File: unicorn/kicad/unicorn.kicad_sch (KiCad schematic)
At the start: 25 parts, among them J1 Conn_01x02, J2 SPI, J3 Conn_01x14_Female, J4 Conn_01x14_Female, U1 L7805, U2 ATmega328-P

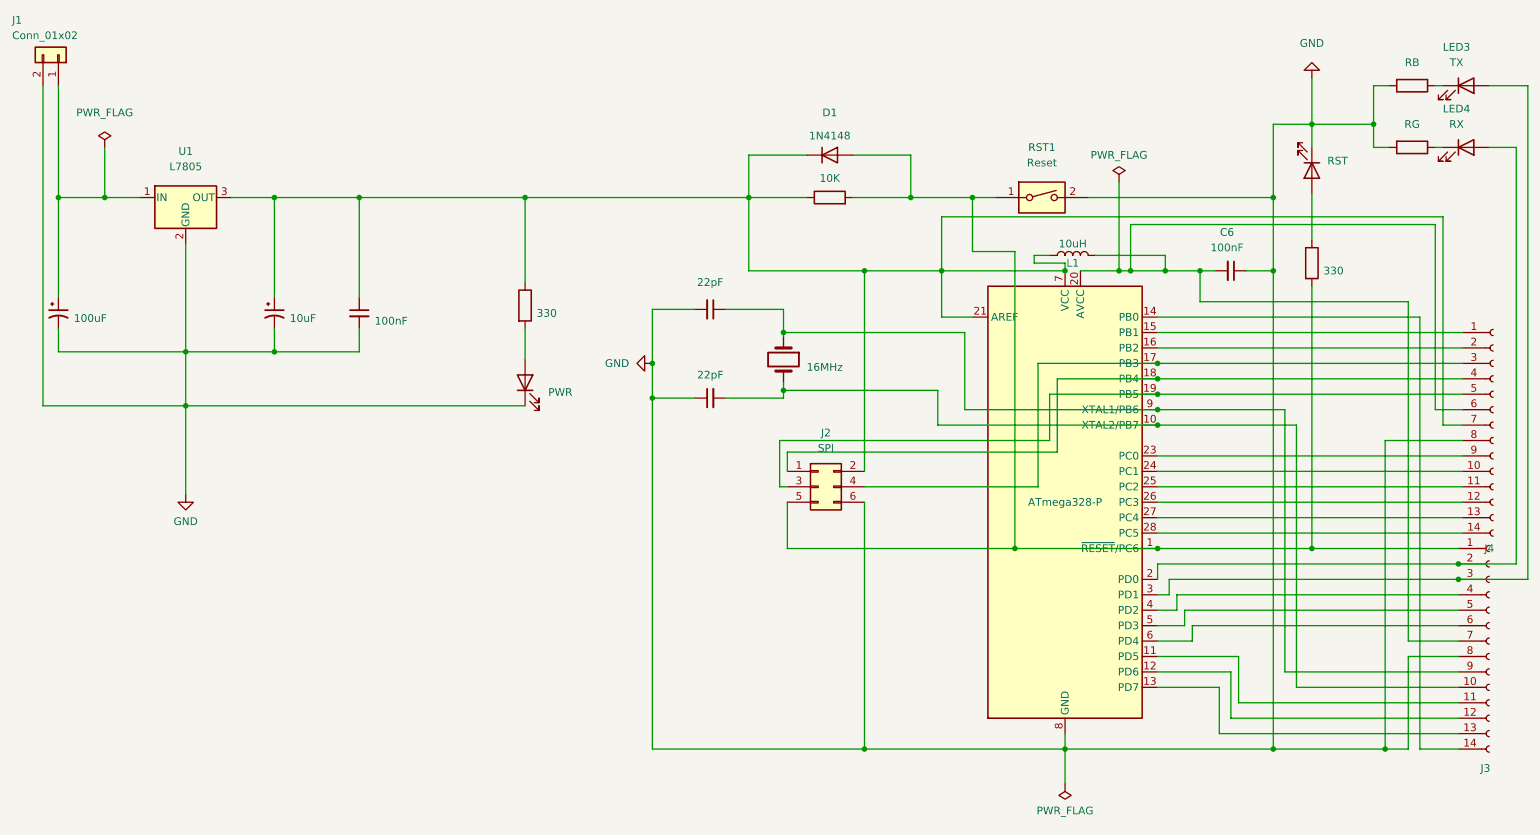
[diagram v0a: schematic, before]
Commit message: Update project to KiCad 8.0
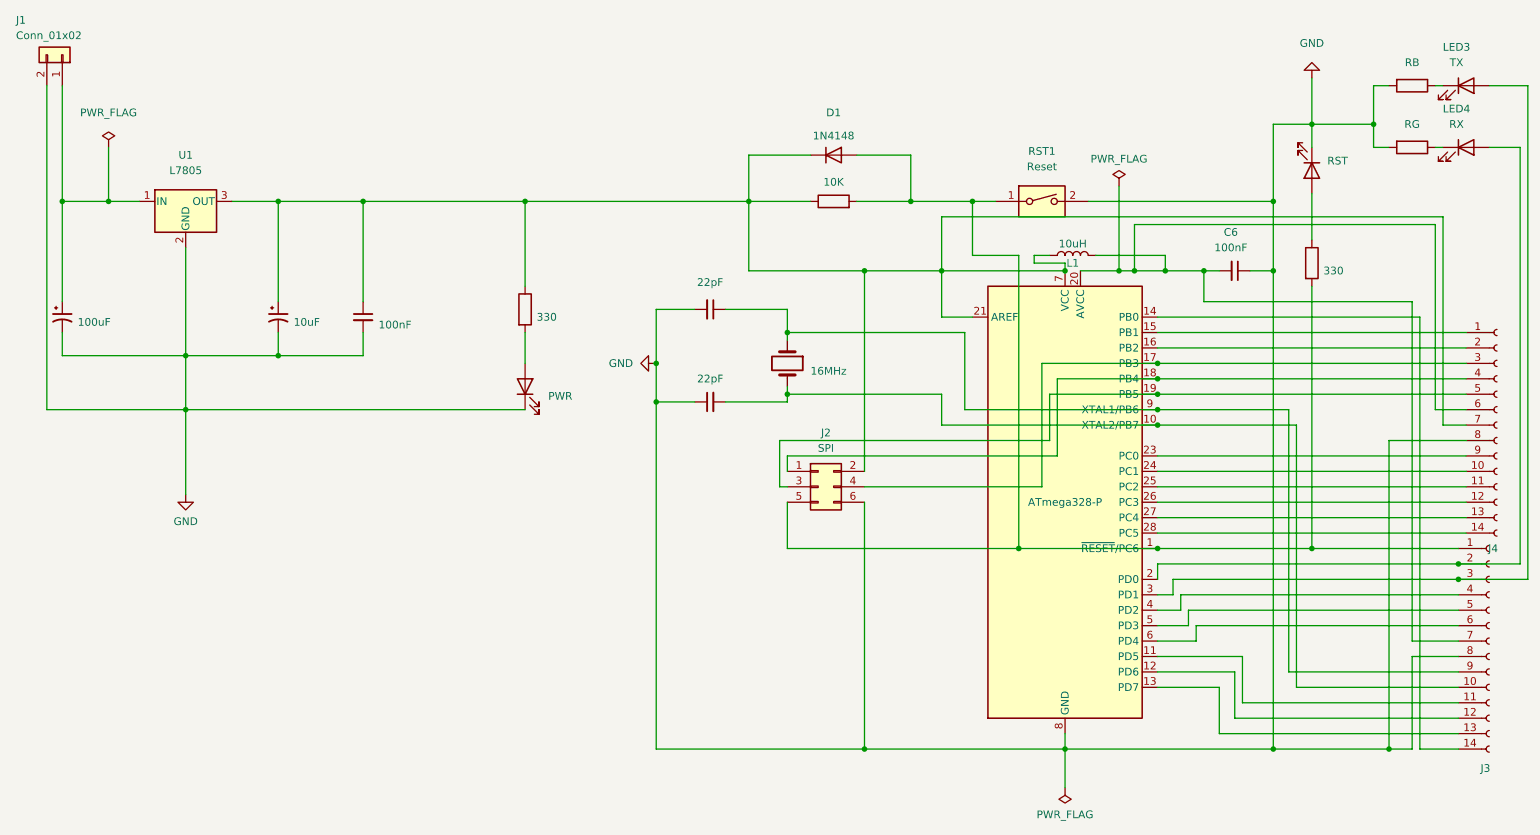
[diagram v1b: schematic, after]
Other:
- moved on the sheet: C6, D1, J1, J4, RST1, U1
